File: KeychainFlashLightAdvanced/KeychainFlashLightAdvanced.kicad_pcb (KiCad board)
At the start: 2 copper layers, 76.2 x 35.6 mm, 4 parts, among them SW1 SW_DPST_x2

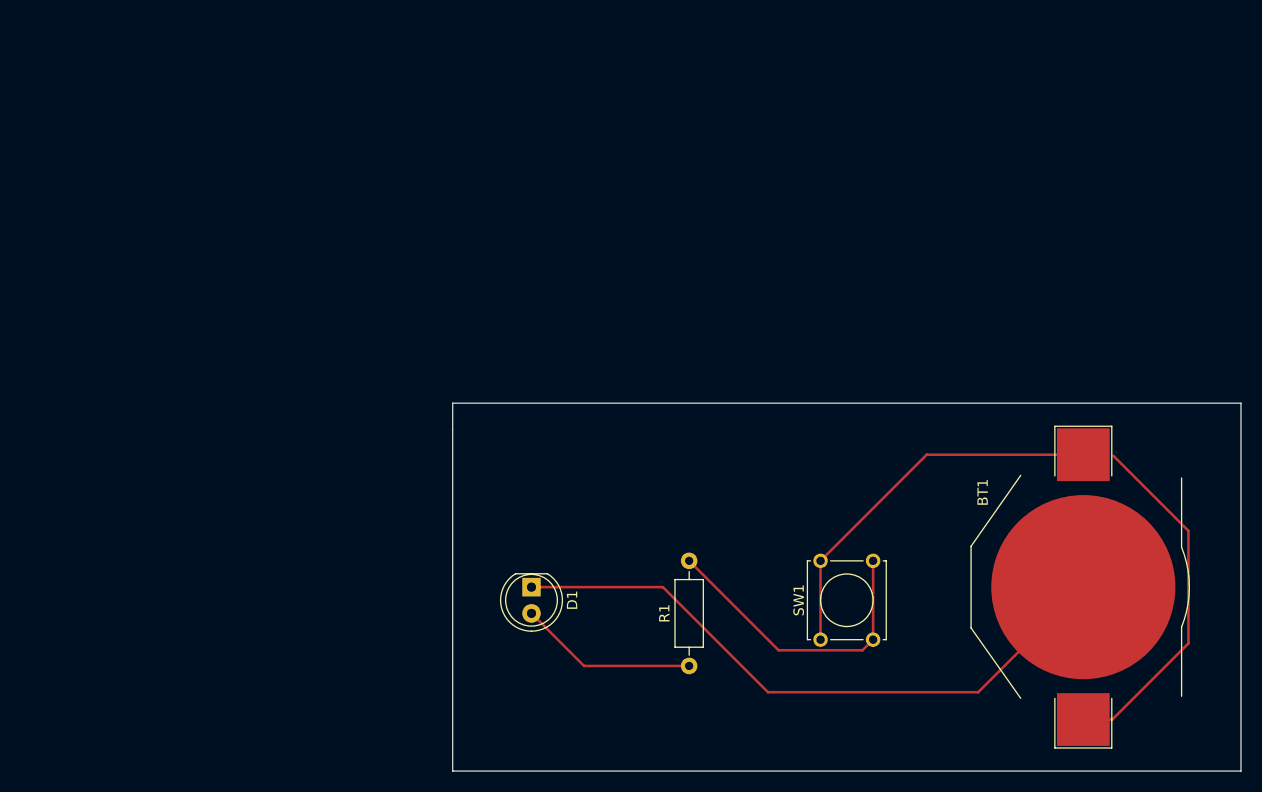
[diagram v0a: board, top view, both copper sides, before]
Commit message: Workshop steps added
Addition of:
Step 4: Importing symbols,
Step 5: Integrating the new button,
Step 6:  Redesigning the board outline and adding a hole,
Step 7: Adding text and pictures to the PCB
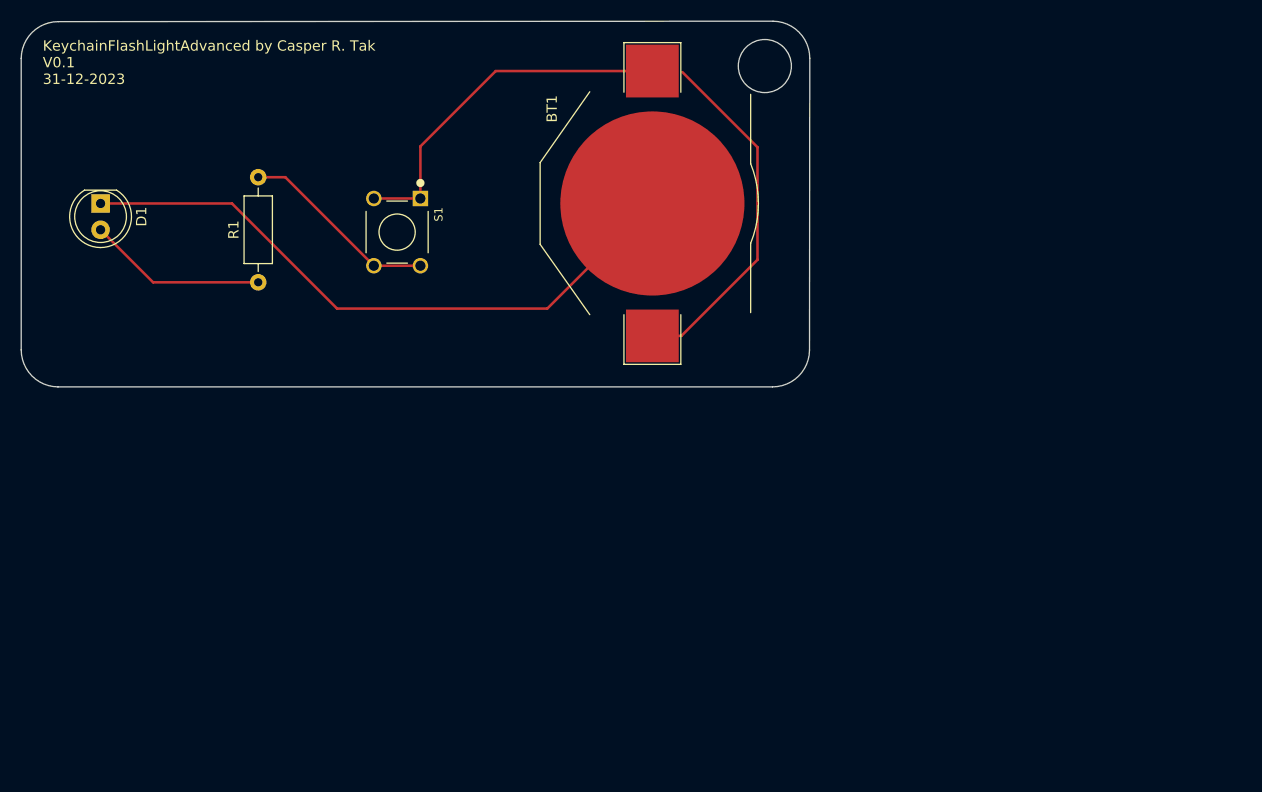
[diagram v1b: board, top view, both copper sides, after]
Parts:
- removed SW1: SW_DPST_x2, Button_Switch_THT:SW_Tactile_Straight_KSA0Axx1LFTR
- added S1: FSM8JH, FSM8JH:SW_FSM8JH, F.Cu at (103.8, 69.8)
- moved BT1 55.8 mm to (128.5, 67.1)
- moved D1 55.8 mm to (75.2, 67.1)
- moved R1 55.8 mm to (90.4, 74.7)
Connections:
- BT1 pad 2: Net-(BT1--) -> +3.3V
- D1 pad 1: Net-(BT1--) -> GND
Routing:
- net Net-(BT1--): track 61.8 -> 0.00 mm
- net (no net): track 0.00 -> 61.8 mm
- net Net-(R1-Pad2): track 29.4 -> 19.2 mm
- net Net-(BT1-+): track 71.6 -> 69.3 mm
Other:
- board size 76.2 x 35.6 mm -> 76.2 x 35.3 mm
- board text added: "KeychainFlashLightAdvanced by Casper R. Tak V0.1 31-12-2023"

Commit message: added step 7 to workshop
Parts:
- added G***: LOGO, LOGO, B.Cu at (86.9, 58.4)
- added REF**: OSHW-Logo2_24.3x20mm_SilkScreen, Symbol:OSHW-Logo2_24.3x20mm_SilkScreen, B.Cu at (128.3, 71.1)
